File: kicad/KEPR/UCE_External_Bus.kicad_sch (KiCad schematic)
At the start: 6 parts, among them J10 Conn_02x40_Odd_Even, J13 PINHD_2x2_Male, J6 Conn_02x20_Odd_Even, J7 Conn_02x08_Odd_Even, J8 Conn_01x08_Pin, J9 Conn_02x40_Odd_Even

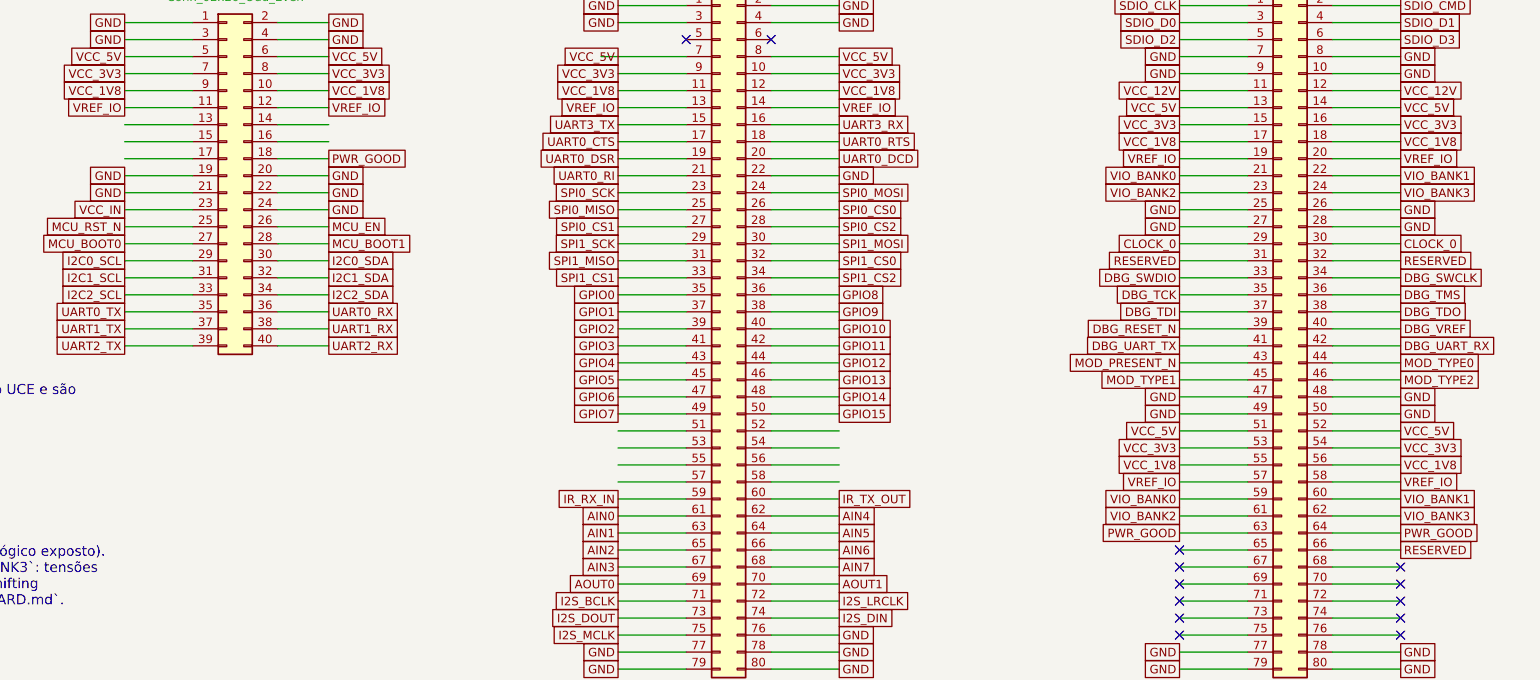
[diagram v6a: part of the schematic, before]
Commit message: Ajustando trilhas
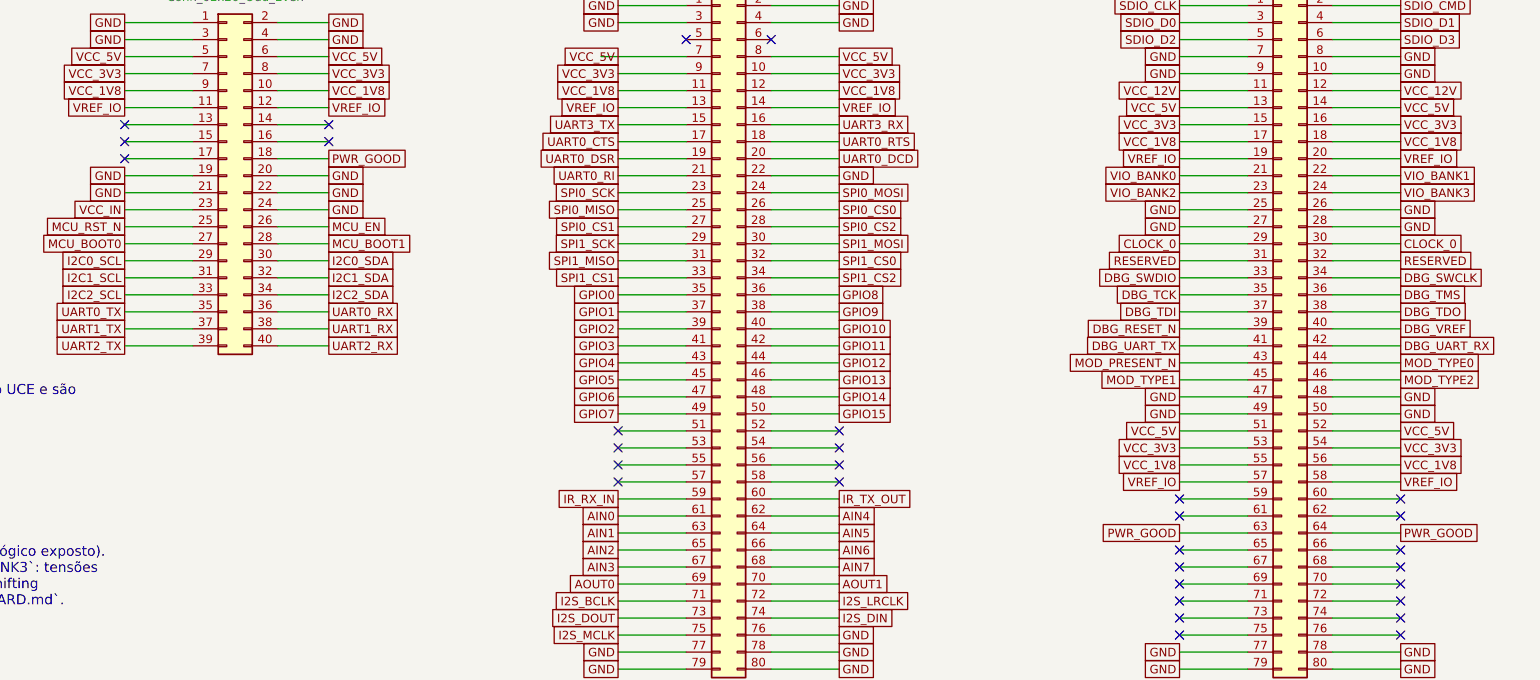
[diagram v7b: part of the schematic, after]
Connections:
- net RESERVED: no longer J10.66 (Pin_66)
- net VIO_BANK0: no longer J10.59 (Pin_59)
- net VIO_BANK1: no longer J10.60 (Pin_60)
- net VIO_BANK2: no longer J10.61 (Pin_61)
- net VIO_BANK3: no longer J10.62 (Pin_62)
- no-connect marks 13 -> 31
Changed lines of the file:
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@@
 	)
 	(no_connect
+		(at 96.52 104.14)
+	)
+	(no_connect
 		(at 254 165.1)
 	)
 	(no_connect
+		(at 203.2 152.4)
+	)
+	(no_connect
+		(at 170.18 152.4)
+	)
+	(no_connect
 		(at 287.02 170.18)
 	)
@@
 	)
 	(no_connect
+		(at 96.52 106.68)
+	)
+	(no_connect
+		(at 203.2 154.94)
+	)
+	(no_connect
 		(at 287.02 175.26)
 	)
 	(no_connect
+		(at 287.02 160.02)
+	)
+	(no_connect
+		(at 254 157.48)
+	)
+	(no_connect
 		(at 193.04 88.9)
 	)
 	(no_connect
+		(at 287.02 165.1)
+	)
+	(no_connect
+		(at 203.2 149.86)
+	)
+	(no_connect
 		(at 287.02 167.64)
 	)
 	(no_connect
+		(at 170.18 154.94)
+	)
+	(no_connect
+		(at 127 104.14)
+	)
+	(no_connect
+		(at 287.02 157.48)
+	)
+	(no_connect
 		(at 254 177.8)
 	)
@@
 	)
 	(no_connect
+		(at 170.18 149.86)
+	)
+	(no_connect
+		(at 203.2 147.32)
+	)
+	(no_connect
+		(at 254 160.02)
+	)
+	(no_connect
+		(at 127 101.6)
+	)
+	(no_connect
+		(at 170.18 147.32)
+	)
+	(no_connect
 		(at 254 170.18)
 	)
 	(no_connect
+		(at 96.52 101.6)
+	)
+	(no_connect
 		(at 254 172.72)
 	)
@@
 		)
 	)
-	(global_label "RESERVED"
-		(shape passive)
-		(at 287.02 165.1 0)
-		(effects
-			(font
-				(size 1.27 1.27)
-			)
-			(justify left bottom)
-		)
-		(property "Intersheetrefs" "${INTERSHEET_REFS}"
-			(at 287.02 165.1 0)
-			(effects
-				(font
-					(size 1.27 1.27)
-				)
-				(hide yes)
-			)
-		)
-	)
 	(global_label "GND"
 		(shape passive)
@@
 		)
 	)
-	(global_label "VIO_BANK2"
-		(shape passive)
-		(at 254 160.02 180)
-		(effects
-			(font
-				(size 1.27 1.27)
-			)
-			(justify right bottom)
-		)
-		(property "Intersheetrefs" "${INTERSHEET_REFS}"
-			(at 254 160.02 0)
-			(effects
-				(font
-					(size 1.27 1.27)
-				)
-				(justify left)
-				(hide yes)
-			)
-		)
-	)
 	(global_label "VCC_1V8"
 		(shape passive)
@@
 		)
 	)
-	(global_label "VIO_BANK0"
-		(shape passive)
-		(at 254 157.48 180)
-		(effects
-			(font
-				(size 1.27 1.27)
-			)
-			(justify right bottom)
-		)
-		(property "Intersheetrefs" "${INTERSHEET_REFS}"
-			(at 254 157.48 0)
-			(effects
-				(font
-					(size 1.27 1.27)
-				)
-				(justify left)
-				(hide yes)
-			)
-		)
-	)
 	(global_label "GND"
 		(shape passive)
@@
 		)
 	)
-	(global_label "VIO_BANK1"
-		(shape passive)
-		(at 287.02 157.48 0)
-		(effects
-			(font
-				(size 1.27 1.27)
-			)
-			(justify left bottom)
-		)
-		(property "Intersheetrefs" "${INTERSHEET_REFS}"
-			(at 287.02 157.48 0)
-			(effects
-				(font
-					(size 1.27 1.27)
-				)
-				(justify left)
-				(hide yes)
-			)
-		)
-	)
 	(global_label "GPIO11"
 		(shape passive)
@@
 				(hide yes)
 			)
-		)
-	)
-	(global_label "VIO_BANK3"
-		(shape passive)
-		(at 287.02 160.02 0)
-		(effects
-			(font
-				(size 1.27 1.27)
-			)
-			(justify left bottom)
-		)
-		(property "Intersheetrefs" "${INTERSHEET_REFS}"
-			(at 287.02 160.02 0)
-			(effects
-				(font
-					(size 1.27 1.27)
-				)
-				(justify left)
-				(hide yes)
-			)

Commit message: mais ajustes de trilha.
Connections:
- net RESERVED: no longer names the net of J10.31 (Pin_31)
- net RESERVED: no longer J10.32 (Pin_32)
- no-connect marks 31 -> 33
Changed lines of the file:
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@@
 	)
 	(no_connect
+		(at 254 121.92)
+	)
+	(no_connect
 		(at 287.02 177.8)
 	)
@@
 		(at 287.02 172.72)
 	)
+	(no_connect
+		(at 287.02 121.92)
+	)
 	(wire
 		(pts
@@
 		)
 	)
-	(global_label "RESERVED"
-		(shape passive)
-		(at 287.02 121.92 0)
-		(effects
-			(font
-				(size 1.27 1.27)
-			)
-			(justify left bottom)
-		)
-		(property "Intersheetrefs" "${INTERSHEET_REFS}"
-			(at 287.02 121.92 0)
-			(effects
-				(font
-					(size 1.27 1.27)
-				)
-				(hide yes)
-			)
-		)
-	)
 	(global_label "SPI1_SCK"
 		(shape passive)
@@
 			(effects
 				(font
-					(size 1.27 1.27)
-				)
-				(hide yes)
-			)
-		)
-	)
-	(global_label "RESERVED"
-		(shape passive)
-		(at 254 121.92 180)
-		(effects
-			(font
-				(size 1.27 1.27)
-			)
-			(justify right bottom)
-		)
-		(property "Intersheetrefs" "${INTERSHEET_REFS}"
-			(at 254 121.92 0)
-			(effects
-				(font
